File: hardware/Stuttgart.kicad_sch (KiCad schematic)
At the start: 0 parts

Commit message: Initial batch of components from the minimal-bom example
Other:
- added sheet RP2354A (rp2354a.kicad_sch)
- added sheet USB Power (usb-power.kicad_sch)
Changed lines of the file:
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@@
 	(generator_version "10.0")
 	(paper "A4")
+	(sheet
+		(at 26.67 31.75)
+		(size 39.37 25.4)
+		(exclude_from_sim no)
+		(in_bom yes)
+		(on_board yes)
+		(dnp no)
+		(fields_autoplaced yes)
+		(stroke
+			(width 0.1524)
+			(type solid)
+		)
+		(fill
+			(color 0 0 0 0)
+		)
+		(property "Sheetname" "RP2354A"
+			(at 26.67 31.0384 0)
+			(show_name no)
+			(do_not_autoplace no)
+			(effects
+				(font
+					(size 1.27 1.27)
+				)
+				(justify left bottom)
+			)
+		)
+		(property "Sheetfile" "rp2354a.kicad_sch"
+			(at 26.67 57.7346 0)
+			(show_name no)
+			(do_not_autoplace no)
+			(effects
+				(font
+					(size 1.27 1.27)
+				)
+				(justify left top)
+			)
+		)
+		(property "Field2" ""
+			(at 26.67 31.75 0)
+			(hide yes)
+			(show_name no)
+			(do_not_autoplace no)
+			(effects
+				(font
+					(size 1.27 1.27)
+				)
+			)
+		)
+		(instances
+			(project "Stuttgart"
+				(path "/6d354744-ce95-4d5c-b7ae-1990dae66f7b"
+					(page "2")
+				)
+			)
+		)
+	)
+	(sheet
+		(at 82.55 35.56)
+		(size 48.26 24.13)
+		(exclude_from_sim no)
+		(in_bom yes)
+		(on_board yes)
+		(dnp no)
+		(fields_autoplaced yes)
+		(stroke
+			(width 0.1524)
+			(type solid)
+		)
+		(fill
+			(color 0 0 0 0)
+		)
+		(property "Sheetname" "USB Power"
+			(at 82.55 34.8484 0)
+			(show_name no)
+			(do_not_autoplace no)
+			(effects
+				(font
+					(size 1.27 1.27)
+				)
+				(justify left bottom)
+			)
+		)
+		(property "Sheetfile" "usb-power.kicad_sch"
+			(at 82.55 60.2746 0)
+			(show_name no)
+			(do_not_autoplace no)
+			(effects
+				(font
+					(size 1.27 1.27)
+				)
+				(justify left top)
+			)
+		)
+		(property "Field2" ""
+			(at 82.55 35.56 0)
+			(hide yes)
+			(show_name no)
+			(do_not_autoplace no)
+			(effects
+				(font
+					(size 1.27 1.27)
+				)
+			)
+		)
+		(instances
+			(project "Stuttgart"
+				(path "/6d354744-ce95-4d5c-b7ae-1990dae66f7b"
+					(page "3")
+				)
+			)
+		)
+	)
 	(sheet_instances
 		(path "/"

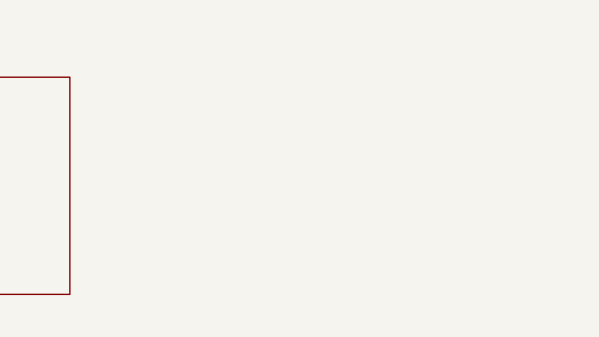
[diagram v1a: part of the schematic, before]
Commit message: Most RP components on board. Core regulator wired up
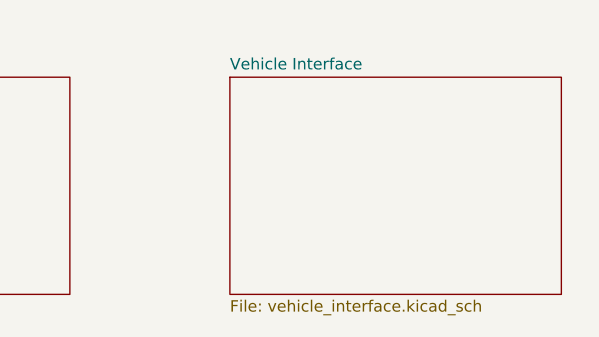
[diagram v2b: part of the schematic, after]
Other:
- added sheet Vehicle Interface (vehicle_interface.kicad_sch)
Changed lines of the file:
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@@
+		)
+	)
+	(sheet
+		(at 148.59 35.56)
+		(size 36.83 24.13)
+		(exclude_from_sim no)
+		(in_bom yes)
+		(on_board yes)
+		(dnp no)
+		(fields_autoplaced yes)
+		(stroke
+			(width 0.1524)
+			(type solid)
+		)
+		(fill
+			(color 0 0 0 0)
+		)
+		(property "Sheetname" "Vehicle Interface"
+			(at 148.59 34.8484 0)
+			(show_name no)
+			(do_not_autoplace no)
+			(effects
+				(font
+					(size 1.27 1.27)
+				)
+				(justify left bottom)
+			)
+		)
+		(property "Sheetfile" "vehicle_interface.kicad_sch"
+			(at 148.59 60.2746 0)
+			(show_name no)
+			(do_not_autoplace no)
+			(effects
+				(font
+					(size 1.27 1.27)
+				)
+				(justify left top)
+			)
+		)
+		(property "Field2" ""
+			(at 148.59 35.56 0)
+			(hide yes)
+			(show_name no)
+			(do_not_autoplace no)
+			(effects
+				(font
+					(size 1.27 1.27)
+				)
+			)
+		)
+		(instances
+			(project "Stuttgart"
+				(path "/6d354744-ce95-4d5c-b7ae-1990dae66f7b"
+					(page "4")
+				)
+			)
 		)
 	)

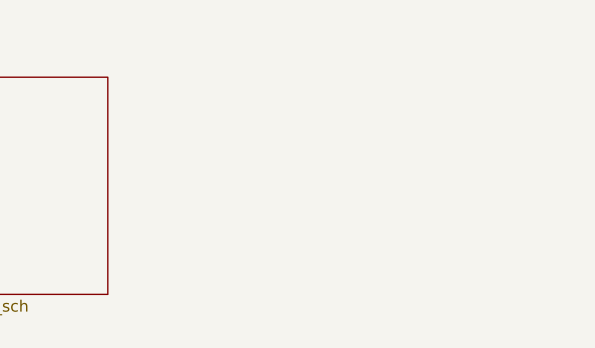
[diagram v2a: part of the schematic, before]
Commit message: Added DCDC IC
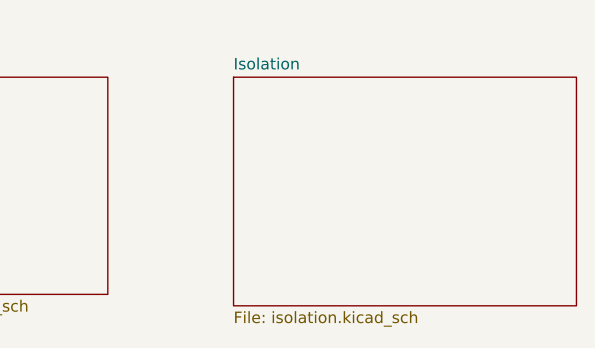
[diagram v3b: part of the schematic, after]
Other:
- added sheet Isolation (isolation.kicad_sch)
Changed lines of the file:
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@@
+		)
+	)
+	(sheet
+		(at 199.39 35.56)
+		(size 38.1 25.4)
+		(exclude_from_sim no)
+		(in_bom yes)
+		(on_board yes)
+		(dnp no)
+		(fields_autoplaced yes)
+		(stroke
+			(width 0.1524)
+			(type solid)
+		)
+		(fill
+			(color 0 0 0 0)
+		)
+		(property "Sheetname" "Isolation"
+			(at 199.39 34.8484 0)
+			(show_name no)
+			(do_not_autoplace no)
+			(effects
+				(font
+					(size 1.27 1.27)
+				)
+				(justify left bottom)
+			)
+		)
+		(property "Sheetfile" "isolation.kicad_sch"
+			(at 199.39 61.5446 0)
+			(show_name no)
+			(do_not_autoplace no)
+			(effects
+				(font
+					(size 1.27 1.27)
+				)
+				(justify left top)
+			)
+		)
+		(instances
+			(project "Stuttgart"
+				(path "/6d354744-ce95-4d5c-b7ae-1990dae66f7b"
+					(page "5")
+				)
+			)
 		)
 	)

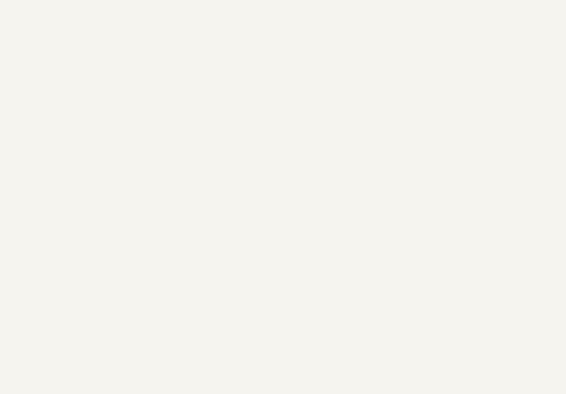
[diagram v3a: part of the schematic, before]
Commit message: Schematic nearly complete. Board size finalised.
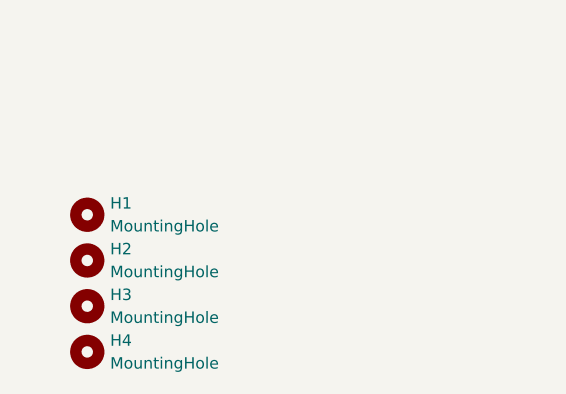
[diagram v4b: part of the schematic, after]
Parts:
- added H1, H2, H3, H4: MountingHole, MountingHole:MountingHole_3.2mm_M3, symbol Mechanical:MountingHole
